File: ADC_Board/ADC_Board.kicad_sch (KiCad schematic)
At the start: 21 parts, among them IC1 UCC12040DVE, IC2 ADS131M04QPWRQ1, IC7 ISO7762FDWR, U5 Nucleo_L432KC

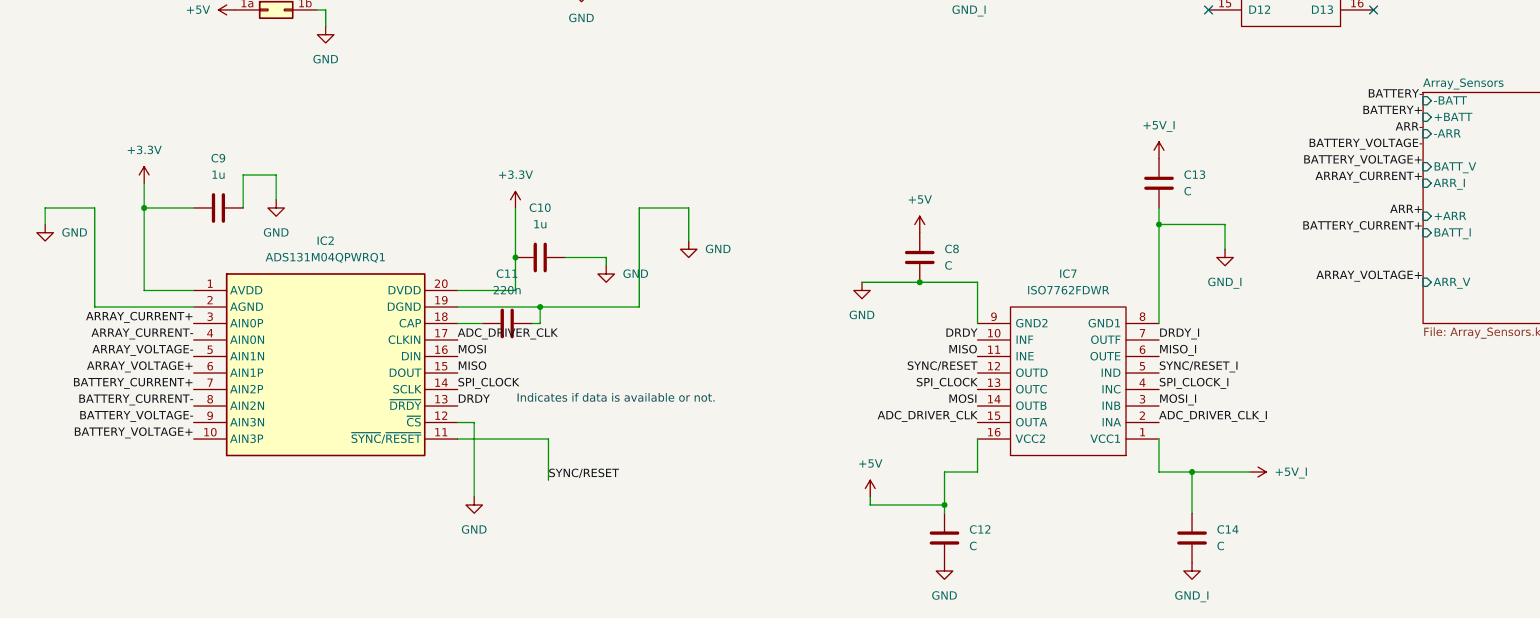
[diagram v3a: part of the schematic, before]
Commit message: Smalll changes made to address ERC issues and review, also updated symbols and ensured all datasheets were linked
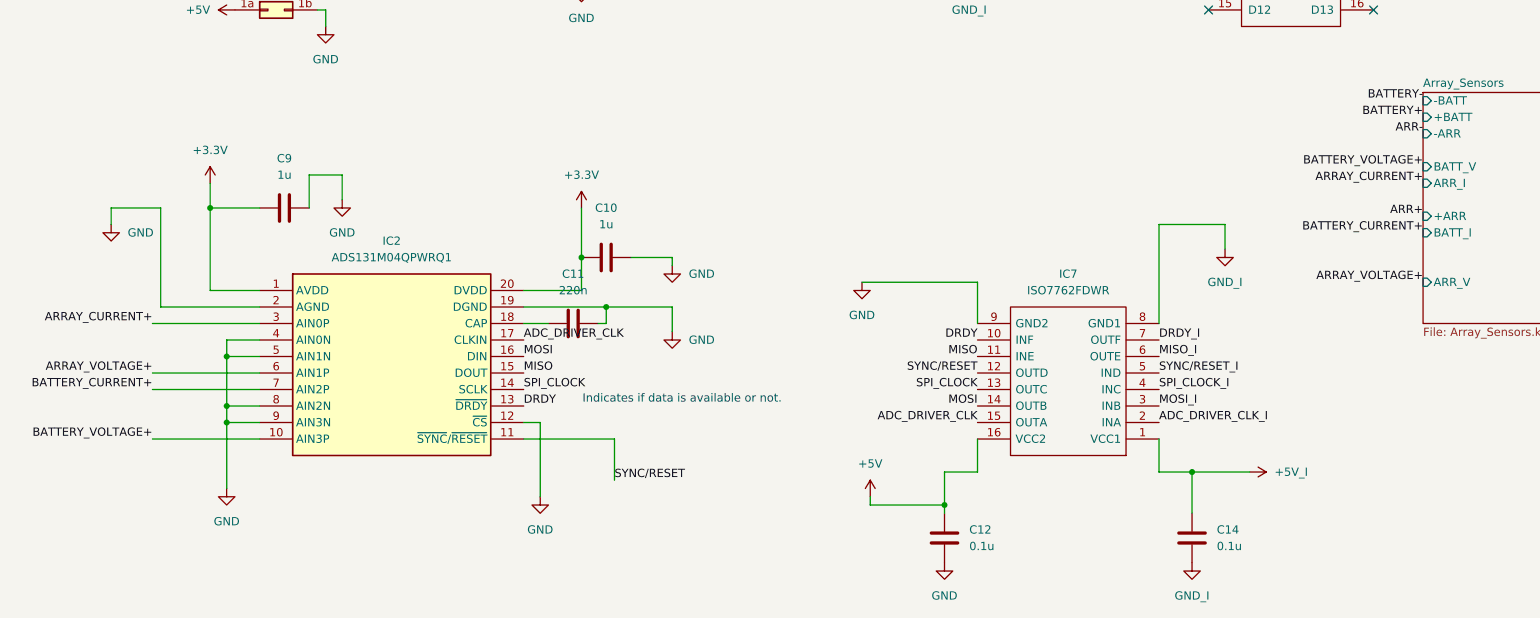
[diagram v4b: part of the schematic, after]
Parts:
- removed C13, C8: C, symbol Device:C
- C12, C14: value C -> 0.1u
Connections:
- net ARRAY_CURRENT- is gone; now on net GND: IC2.4 (AIN0N)
- net ARRAY_VOLTAGE- is gone; now on net GND: IC2.5 (AIN1N)
- net BATTERY_CURRENT- is gone; now on net GND: IC2.8 (AIN2N)
- net BATTERY_VOLTAGE- is gone; now on net GND: IC2.9 (AIN3N)
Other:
- moved on the sheet: C10, C11, C9, IC2

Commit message: Created Layout
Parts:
- removed 5v_Input: Banana_Cable_1, symbol Connector_Generic:Conn_02x01_Row_Letter_Last
- removed ARR+, ARR-, BATTERY+, BATTERY-: TestPoint, symbol Connector:TestPoint
- removed ARRAY_INPUT1: Banana_Cable_2, symbol Connector_Generic:Conn_02x01_Row_Letter_Last
- removed BATTERY_INPUT1: Banana_Cable_3, symbol Connector_Generic:Conn_02x01_Row_Letter_Last
- removed C6: C, symbol Device:C
- added J1, J2, J3, J4, J5, J6: Conn_01x01_Pin, UTSVT_Connectors:Banana_Jack_1_Pin_4mm, symbol Connector:Conn_01x01_Pin
- C10, C11, C12, C14, C7, C9: footprint (none) -> Capacitor_SMD:C_0805_2012Metric
- C5: value C -> 10u; footprint (none) -> Capacitor_SMD:C_0805_2012Metric
- IC1, IC7: footprint SOIC127P1030X265-16N -> ISO7762FDWR:SOIC127P1030X265-16N
- IC2: footprint SOP65P640X120-20N -> ADS131M04QPWRQ1:SOP65P640X120-20N
- U5: footprint (none) -> UTSVT_Special:NucleoL432KC
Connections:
- net +5V: now also J3.1 (Pin_1)
- net ARR+: now also J1.1 (Pin_1)
- net ARR-: now also J4.1 (Pin_1)
- net BATTERY+: now also J2.1 (Pin_1)
- net BATTERY-: now also J5.1 (Pin_1)
- net GND: now also J6.1 (Pin_1)
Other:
- note added: "5V_INPUT"
- note added: "ARRAY_INPUT"
- note added: "BATTERY_INPUT"

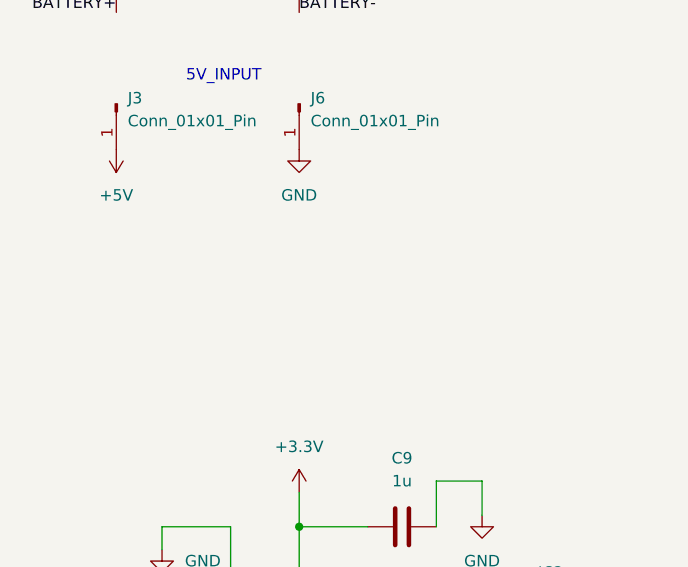
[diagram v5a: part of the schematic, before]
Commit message: Added 3.3v input power to schematic
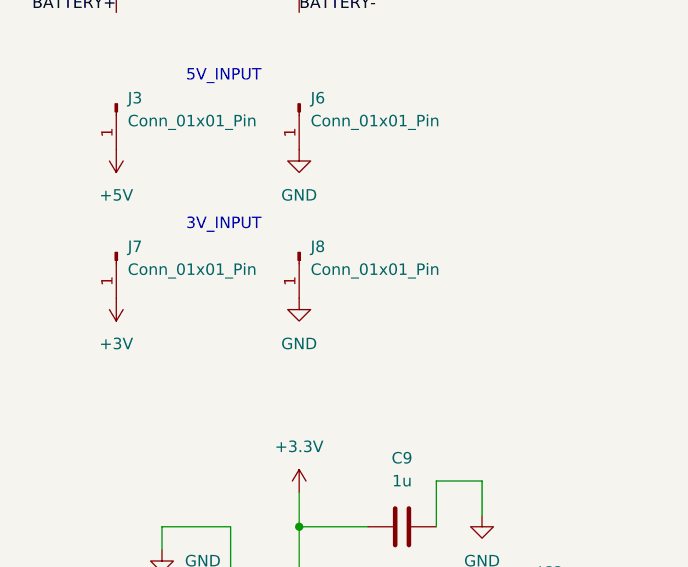
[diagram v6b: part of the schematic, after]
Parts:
- added J7, J8: Conn_01x01_Pin, UTSVT_Connectors:Banana_Jack_1_Pin_4mm, symbol Connector:Conn_01x01_Pin
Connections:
- net GND: now also J8.1 (Pin_1)
- new net +3V: J7.1 (Pin_1)
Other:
- note added: "3V_INPUT"

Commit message: Added a few small things to address reviews. Made a lot of improvements to readability.
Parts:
- added C6, C8: 0.1u, Capacitor_SMD:C_0805_2012Metric, symbol Device:C
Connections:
- net +3V is gone; now on net +3.3V: J7.1 (Pin_1)
- net +5V: now also C5.1, C8.2; no longer C5.2
- net +5V_I: now also C7.2, C6.2; no longer C7.1
- net GND: now also C5.2, C8.1; no longer C5.1
- net GND_I: now also C7.1, C6.1; no longer C7.2
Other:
- note added: "5V ISOLATOR"
- note added: "ADC"
- note added: "SPI ISOLATOR"
- moved on the sheet: C10, C11, C12, C14, C7, C9, IC1, IC2, IC7, J2, J3, J5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
